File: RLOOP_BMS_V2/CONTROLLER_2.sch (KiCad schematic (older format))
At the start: 20 parts, among them IC3 ATA6870N-PLQW-1

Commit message: Footprint work
starting to assign footprints to parts
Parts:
- C10, C11, C12, C13, C14, C15, C3, C4, C5, C6, C7, C8, C9: footprint (none) -> Capacitors_SMD:C_0603
- R10, R11, R8, R9: footprint (none) -> Resistors_SMD:R_0603
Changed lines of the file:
@@
 F 0 "C8" H 8100 1950 50  0000 L CNN
 F 1 "100 nF / 50V/ 10% / SMD 0603" H 8500 1950 50  0000 L CNN
-F 2 "" H 8388 1800 50  0001 C CNN
+F 2 "Capacitors_SMD:C_0603" H 8388 1800 50  0001 C CNN
 F 3 "" H 8350 1950 50  0001 C CNN
 	1    8350 1950
@@
 F 0 "C9" H 8100 2250 50  0000 L CNN
 F 1 "100 nF / 50V/ 10% / SMD 0603" H 8500 2250 50  0000 L CNN
-F 2 "" H 8388 2100 50  0001 C CNN
+F 2 "Capacitors_SMD:C_0603" H 8388 2100 50  0001 C CNN
 F 3 "" H 8350 2250 50  0001 C CNN
 	1    8350 2250
@@
 F 0 "C10" H 8100 2550 50  0000 L CNN
 F 1 "100 nF / 50V/ 10% / SMD 0603" H 8500 2550 50  0000 L CNN
-F 2 "" H 8388 2400 50  0001 C CNN
+F 2 "Capacitors_SMD:C_0603" H 8388 2400 50  0001 C CNN
 F 3 "" H 8350 2550 50  0001 C CNN
 	1    8350 2550
@@
 F 0 "C11" H 8100 2850 50  0000 L CNN
 F 1 "100 nF / 50V/ 10% / SMD 0603" H 8500 2850 50  0000 L CNN
-F 2 "" H 8388 2700 50  0001 C CNN
+F 2 "Capacitors_SMD:C_0603" H 8388 2700 50  0001 C CNN
 F 3 "" H 8350 2850 50  0001 C CNN
 	1    8350 2850
@@
 F 0 "C12" H 8100 3150 50  0000 L CNN
 F 1 "100 nF / 50V/ 10% / SMD 0603" H 8500 3150 50  0000 L CNN
-F 2 "" H 8388 3000 50  0001 C CNN
+F 2 "Capacitors_SMD:C_0603" H 8388 3000 50  0001 C CNN
 F 3 "" H 8350 3150 50  0001 C CNN
 	1    8350 3150
@@
 F 0 "C13" H 8100 3450 50  0000 L CNN
 F 1 "100 nF / 50V/ 10% / SMD 0603" H 8500 3450 50  0000 L CNN
-F 2 "" H 8388 3300 50  0001 C CNN
+F 2 "Capacitors_SMD:C_0603" H 8388 3300 50  0001 C CNN
 F 3 "" H 8350 3450 50  0001 C CNN
 	1    8350 3450
@@
 F 0 "R9" V 6980 4350 50  0000 C CNN
 F 1 "121K / 0.1W / 1% / SMD 0603" V 7050 4850 50  0000 C CNN
-F 2 "" V 6830 4350 50  0001 C CNN
+F 2 "Resistors_SMD:R_0603" V 6830 4350 50  0001 C CNN
 F 3 "" H 6900 4350 50  0001 C CNN
 	1    6900 4350
@@
 F 0 "R11" V 10030 4050 50  0000 C CNN
 F 1 "10K / .1 W / 1% / SMD 0603" H 9300 4050 50  0000 C CNN
-F 2 "" V 9880 4050 50  0001 C CNN
+F 2 "Resistors_SMD:R_0603" V 9880 4050 50  0001 C CNN
 F 3 "" H 9950 4050 50  0001 C CNN
 	1    9950 4050
@@
 F 0 "R10" V 9080 4050 50  0000 C CNN
 F 1 "10K / .1 W / 1% / SMD 0603" H 9200 4200 50  0000 C CNN
-F 2 "" V 8930 4050 50  0001 C CNN
+F 2 "Resistors_SMD:R_0603" V 8930 4050 50  0001 C CNN
 F 3 "" H 9000 4050 50  0001 C CNN
 	1    9000 4050
@@
 F 0 "C15" H 9575 4650 50  0000 L CNN
 F 1 "100n" H 9250 4550 50  0000 L CNN
-F 2 "" H 9588 4400 50  0001 C CNN
+F 2 "Capacitors_SMD:C_0603" H 9588 4400 50  0001 C CNN
 F 3 "" H 9550 4550 50  0001 C CNN
 	1    9550 4550
@@
 F 0 "C14" H 8475 4650 50  0000 L CNN
 F 1 "100n" H 8200 4450 50  0000 L CNN
-F 2 "" H 8488 4400 50  0001 C CNN
+F 2 "Capacitors_SMD:C_0603" H 8488 4400 50  0001 C CNN
 F 3 "" H 8450 4550 50  0001 C CNN
 	1    8450 4550
@@
 F 0 "R8" V 2730 6900 50  0000 C CNN
 F 1 "10" V 2650 6900 50  0000 C CNN
-F 2 "" V 2580 6900 50  0001 C CNN
+F 2 "Resistors_SMD:R_0603" V 2580 6900 50  0001 C CNN
 F 3 "" H 2650 6900 50  0001 C CNN
 	1    2650 6900
@@
 F 0 "C7" H 6775 2100 50  0000 L CNN
 F 1 "100nF / 50V / 10% / SMD 0603" H 5400 2150 50  0000 L CNN
-F 2 "" H 6788 1850 50  0001 C CNN
+F 2 "Capacitors_SMD:C_0603" H 6788 1850 50  0001 C CNN
 F 3 "" H 6750 2000 50  0001 C CNN
 	1    6750 2000
@@
 F 0 "C4" H 3225 7250 50  0000 L CNN
 F 1 "10uF / 25V / 20% / SMD 1206" H 1750 7150 50  0000 L CNN
-F 2 "" H 3238 7000 50  0001 C CNN
+F 2 "Capacitors_SMD:C_0603" H 3238 7000 50  0001 C CNN
 F 3 "" H 3200 7150 50  0001 C CNN
 	1    3200 7150
@@
 F 0 "C6" H 5475 1800 50  0000 L CNN
 F 1 "100n / 50V / 10% / SMD 0603" H 5250 1900 50  0000 L CNN
-F 2 "" H 5488 1550 50  0001 C CNN
+F 2 "Capacitors_SMD:C_0603" H 5488 1550 50  0001 C CNN
 F 3 "" H 5450 1700 50  0001 C CNN
 	1    5450 1700
@@
 F 0 "C5" H 3275 2900 50  0000 L CNN
 F 1 "100nF / 50V / 10% / SMD 0603" H 3275 2700 50  0000 L CNN
-F 2 "" H 3288 2650 50  0001 C CNN
+F 2 "Capacitors_SMD:C_0603" H 3288 2650 50  0001 C CNN
 F 3 "" H 3250 2800 50  0001 C CNN
 	1    3250 2800
@@
 F 0 "C3" H 2725 2900 50  0000 L CNN
 F 1 "10uF / 25V / 20% / SMD 1206" H 1300 2800 50  0000 L CNN
-F 2 "" H 2738 2650 50  0001 C CNN
+F 2 "Capacitors_SMD:C_0603" H 2738 2650 50  0001 C CNN
 F 3 "" H 2700 2800 50  0001 C CNN
 	1    2700 2800

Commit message: footprint and layout work WIP
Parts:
- IC3: footprint (none) -> rLoop_Footprints:ATA6870-QFN48
- TH1, TH2: footprint (none) -> Resistors_SMD:R_0603
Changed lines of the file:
@@
 F 0 "IC3" H 6300 5200 60  0000 C CNN
 F 1 "ATA6870N-PLQW-1" H 6650 5100 60  0000 C CNN
-F 2 "" H 5550 3400 60  0001 C CNN
+F 2 "rLoop_Footprints:ATA6870-QFN48" H 5550 3400 60  0001 C CNN
 F 3 "" H 5550 3400 60  0001 C CNN
 	1    5600 3400
@@
 F 0 "TH2" V 9775 4550 50  0000 C CNN
 F 1 "NTCS0603E3103JLT" H 10450 4550 50  0000 C CNN
-F 2 "" H 9950 4600 50  0001 C CNN
+F 2 "Resistors_SMD:R_0603" H 9950 4600 50  0001 C CNN
 F 3 "" H 9950 4600 50  0001 C CNN
 	1    9950 4550
@@
 F 0 "TH1" V 8825 4550 50  0000 C CNN
 F 1 "NTCS0603E3103JLT" H 9000 4350 50  0000 C CNN
-F 2 "" H 9000 4600 50  0001 C CNN
+F 2 "Resistors_SMD:R_0603" H 9000 4600 50  0001 C CNN
 F 3 "" H 9000 4600 50  0001 C CNN
 	1    9000 4550

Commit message: board layout wip
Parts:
- C3, C4: footprint Capacitors_SMD:C_0603 -> Capacitors_SMD:C_1206
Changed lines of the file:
@@
 F 0 "C4" H 3225 7250 50  0000 L CNN
 F 1 "10uF / 25V / 20% / SMD 1206" H 1750 7150 50  0000 L CNN
-F 2 "Capacitors_SMD:C_0603" H 3238 7000 50  0001 C CNN
+F 2 "Capacitors_SMD:C_1206" H 3238 7000 50  0001 C CNN
 F 3 "" H 3200 7150 50  0001 C CNN
 	1    3200 7150
@@
 F 0 "C3" H 2725 2900 50  0000 L CNN
 F 1 "10uF / 25V / 20% / SMD 1206" H 1300 2800 50  0000 L CNN
-F 2 "Capacitors_SMD:C_0603" H 2738 2650 50  0001 C CNN
+F 2 "Capacitors_SMD:C_1206" H 2738 2650 50  0001 C CNN
 F 3 "" H 2700 2800 50  0001 C CNN
 	1    2700 2800

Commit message: WIP
See if it's even possible
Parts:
- removed C14, C15: 100n, Capacitors_SMD:C_0603, symbol C
- removed C5, C7: 100nF / 50V / 10% / SMD 0603, Capacitors_SMD:C_0603, symbol C
- removed C6: 100n / 50V / 10% / SMD 0603, Capacitors_SMD:C_0603, symbol C
- removed IC3: ATA6870N-PLQW-1, rLoop_Footprints:ATA6870-QFN48, symbol ATA6870N-PLQW-1
- removed R10, R11: 10K / .1 W / 1% / SMD 0603, Resistors_SMD:R_0603, symbol R
- removed R8: 10, Resistors_SMD:R_0603, symbol R
- removed R9: 121K / 0.1W / 1% / SMD 0603, Resistors_SMD:R_0603, symbol R
- removed TH1, TH2: NTCS0603E3103JLT, Resistors_SMD:R_0603, symbol Thermistor_NTC
- added U2: bq76PL536A_HTQFP, symbol bq76PL536A_HTQFP
- C3, C4: value 10uF / 25V / 20% / SMD 1206 -> 2.2 uF / 50V/ 10% / SMD 0603; footprint Capacitors_SMD:C_1206 -> (none)
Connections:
- net labels added: 5V_2, CS_N, CS_S, SCLK_N, SCLK_S, SDI_N, SDI_S, SDO_N, SDO_S
- net labels removed: CLK_IN, CLK_OUT, IRQ_IN, IRQ_OUT, SPI_MISO_LWR, SPI_MISO_UP, SPI_MOSI_LWR, SPI_MOSI_UP, SPI_NCS_LWR, SPI_NCS_UP, SPI_SCK_LWR, SPI_SCK_UP, VDDHVM, VDDHVP, ~PD_IN, ~PD_OUT
- wire segments 86 -> 52
- no-connect marks 3 -> 9
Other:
- moved on the sheet: C10, C11, C12, C13, C8, C9

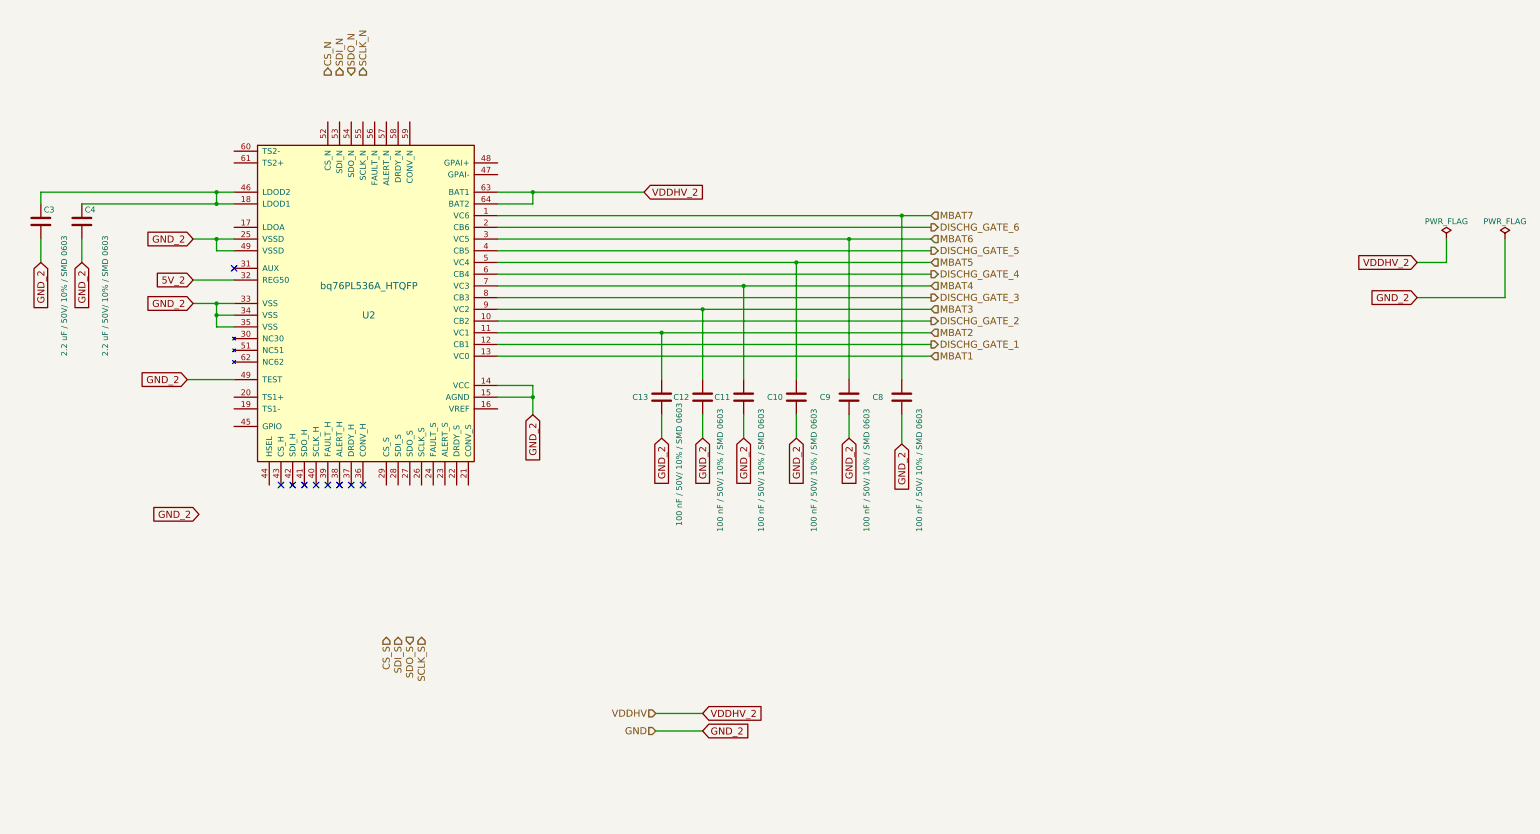
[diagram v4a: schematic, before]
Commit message: Ti BMS WIP
Getting there. Need to add temp sensors, fan control, and an LDO for the
SPI ISO supply.
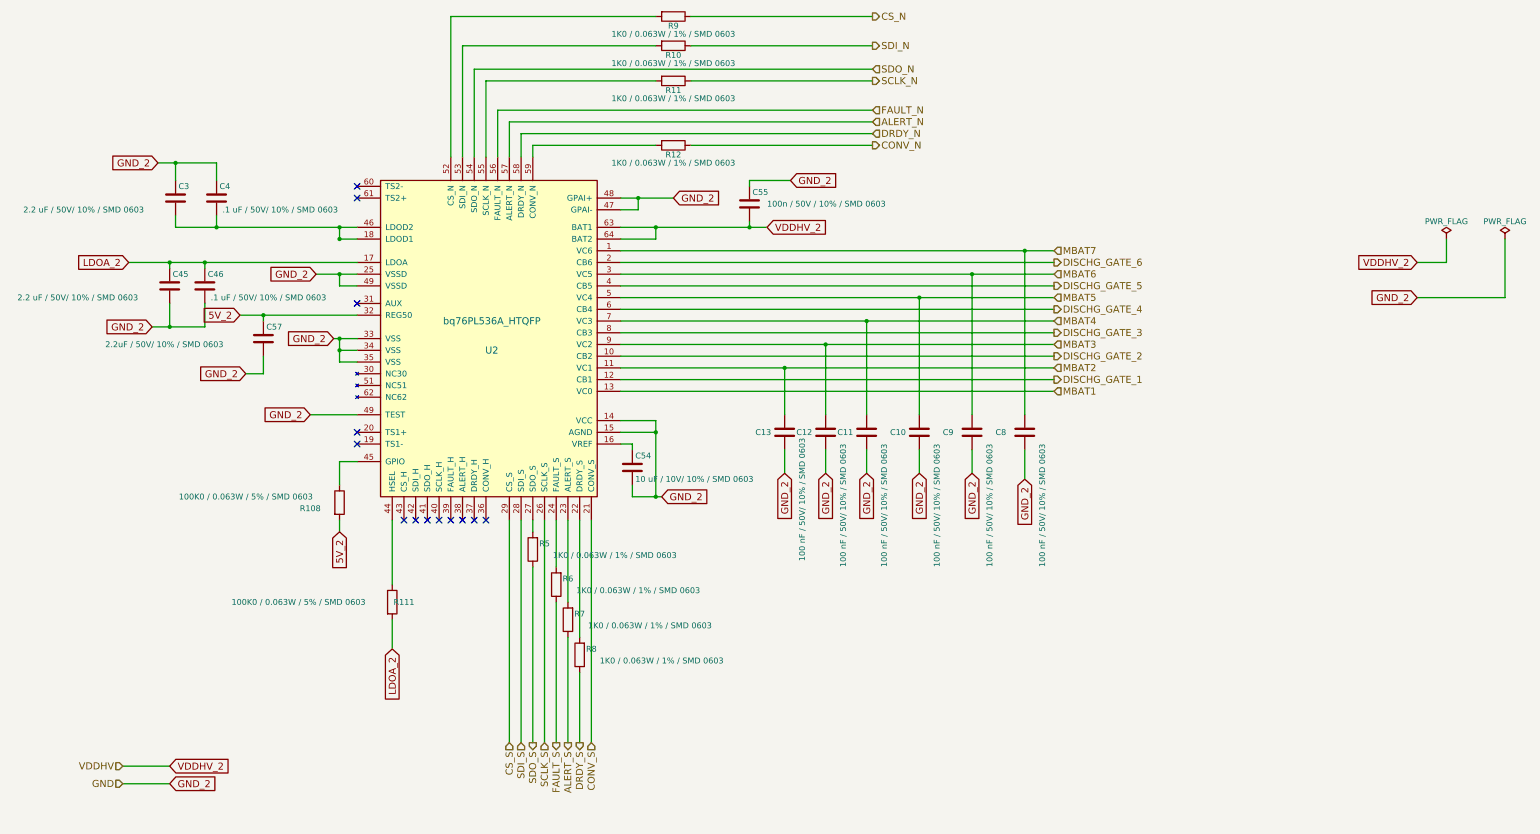
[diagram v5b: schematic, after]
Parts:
- added C45: 2.2 uF / 50V/ 10% / SMD 0603, Capacitors_SMD:C_0603, symbol C
- added C46: .1 uF / 50V/ 10% / SMD 0603, Capacitors_SMD:C_0603, symbol C
- added C54: 10 uF / 10V/ 10% / SMD 0603, Capacitors_SMD:C_0603, symbol C
- added C55: 100n / 50V / 10% / SMD 0603, Capacitors_SMD:C_0603, symbol C
- added C57: 2.2uF / 50V/ 10% / SMD 0603, Capacitors_SMD:C_0603, symbol C
- added R10, R11, R12, R5, R6, R7, R8, R9: 1K0 / 0.063W / 1% / SMD 0603, Resistors_SMD:R_0603, symbol R
- added R108, R111: 100K0 / 0.063W / 5% / SMD 0603, Resistors_SMD:R_0603, symbol R
- C3: footprint (none) -> Capacitors_SMD:C_0603
- C4: value 2.2 uF / 50V/ 10% / SMD 0603 -> .1 uF / 50V/ 10% / SMD 0603; footprint (none) -> Capacitors_SMD:C_0603
- U2: footprint (none) -> rLoop_Footprints:bq76pl536a
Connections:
- net 5V_2: now also C57.1, R108.2
- net CS_N: now also R9.1
- net CS_S: now also U2.29 (CS_S)
- net GND_2: now also C3.1, C4.1, U2.47 (GPAI-), U2.48 (GPAI+), C45.2, C46.2, C54.2, C55.1, C57.2; no longer C3.2, C4.2
- net SCLK_N: now also R11.1
- net SCLK_S: now also U2.26 (SCLK_S)
- net SDI_N: now also R10.1
- net SDI_S: now also U2.28 (SDI_S)
- net SDO_N: now also U2.54 (SDO_N)
- net SDO_S: now also R5.1
- net VDDHV_2: now also C55.2
- net at U2.16 (VREF): now also C54.1
- net LDOA_2: now reaches U2.17 (LDOA)
- net LDOA_2: now also C45.1, C46.1, R111.2
- net at U2.18 (LDOD1), U2.46 (LDOD2): now also C3.2, C4.2; no longer C3.1, C4.1
- net CONV_S: now reaches U2.21 (CONV_S)
- net at U2.22 (DRDY_S): now also R8.2
- net at U2.23 (ALERT_S): now also R7.2
- net at U2.24 (FAULT_S): now also R6.2
- net at U2.27 (SDO_S): now also R5.2
- net at U2.44 (HSEL): now also R111.1
- net at U2.45 (GPIO): now also R108.1
- net at U2.52 (CS_N): now also R9.2
- net at U2.53 (SDI_N): now also R10.2
- net at U2.55 (SCLK_N): now also R11.2
- net FAULT_N: now reaches U2.56 (FAULT_N)
- net ALERT_N: now reaches U2.57 (ALERT_N)
- net DRDY_N: now reaches U2.58 (DRDY_N)
- net at U2.59 (CONV_N): now also R12.2
- new net ALERT_S: R7.1
- new net CONV_N: R12.1
- new net DRDY_S: R8.1
- new net FAULT_S: R6.1
- no-connect marks 9 -> 13
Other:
- moved on the sheet: C10, C11, C12, C13, C3, C4, C8, C9, U2

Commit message: More WIP on BMS v2.5
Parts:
- added C? (x2): .047 uF / 50V/ 10% / SMD 0603, Capacitors_SMD:C_0603, symbol C
- added R? (x4): 1.82k / 0.063W / 1% / SMD0603, symbol R
- added TH? (x2): 10k / 1% / 3454K / SMD0603, symbol Thermistor_NTC
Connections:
- net 5V_2: now also C?.1, C?.2, TH?.1, TH?.2
- net at U2.19 (TS1-): now also R?.1
- net at U2.20 (TS1+): now also C?.1, R?.1, R?.2
- net at U2.60 (TS2-): now also R?.1
- net at U2.61 (TS2+): now also C?.2, R?.1, R?.2
- new net: R?.2, TH?.2
- new net: R?.2, TH?.1
- no-connect marks 13 -> 9
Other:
- moved on the sheet: C10, C11, C12, C13, C3, C4, C45, C46, C54, C55, C57, C8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

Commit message: More BMS v2.5 WIP
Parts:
- R116, R117, R118, R119: renamed from R?; footprint (none) -> Resistors_SMD:R_0603
- TH3, TH4: renamed from TH?; footprint (none) -> Resistors_SMD:R_0603
- gave numbers to parts that had none: 2
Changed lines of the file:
@@
 $Descr A4 11693 8268
 encoding utf-8
-Sheet 5 9
+Sheet 5 10
 Title ""
 Date ""
@@
 $EndComp
 $Comp
-L C C?
+L C C61
 U 1 1 592E67EF
 P 3550 1650
-F 0 "C?" H 3575 1750 50  0000 L CNN
+F 0 "C61" H 3575 1750 50  0000 L CNN
 F 1 ".047 uF / 50V/ 10% / SMD 0603" H 3600 1550 50  0000 L CNN
 F 2 "Capacitors_SMD:C_0603" H 3588 1500 50  0001 C CNN
@@
 $EndComp
 $Comp
-L R R?
+L R R119
 U 1 1 592E68AE
 P 4000 2200
-F 0 "R?" V 3900 2200 50  0000 C CNN
+F 0 "R119" V 3900 2200 50  0000 C CNN
 F 1 "1.82k / 0.063W / 1% / SMD0603" V 3800 2500 50  0000 C CNN
-F 2 "" V 3930 2200 50  0001 C CNN
+F 2 "Resistors_SMD:R_0603" V 3930 2200 50  0001 C CNN
 F 3 "" H 4000 2200 50  0001 C CNN
 	1    4000 2200
@@
 $EndComp
 $Comp
-L R R?
+L R R118
 U 1 1 592E6D61
 P 3350 2200
-F 0 "R?" V 3450 2200 50  0000 C CNN
+F 0 "R118" V 3450 2200 50  0000 C CNN
 F 1 "1.82k / 0.063W / 1% / SMD0603" V 3550 2550 50  0000 C CNN
-F 2 "" V 3280 2200 50  0001 C CNN
+F 2 "Resistors_SMD:R_0603" V 3280 2200 50  0001 C CNN
 F 3 "" H 3350 2200 50  0001 C CNN
 	1    3350 2200
@@
 $EndComp
 $Comp
-L Thermistor_NTC TH?
+L Thermistor_NTC TH4
 U 1 1 592E75DB
 P 3150 1650
-F 0 "TH?" H 2900 1700 50  0000 C CNN
+F 0 "TH4" H 2900 1700 50  0000 C CNN
 F 1 "10k / 1% / 3454K / SMD0603" H 2350 1600 50  0000 C CNN
-F 2 "" H 3150 1700 50  0001 C CNN
+F 2 "Resistors_SMD:R_0603" H 3150 1700 50  0001 C CNN
 F 3 "" H 3150 1700 50  0001 C CNN
 	1    3150 1650
@@
 Connection ~ 3150 1300
 $Comp
-L R R?
+L R R117
 U 1 1 592E7F7D
 P 2550 4400
-F 0 "R?" V 2650 4400 50  0000 C CNN
+F 0 "R117" V 2650 4400 50  0000 C CNN
 F 1 "1.82k / 0.063W / 1% / SMD0603" V 2750 5000 50  0000 C CNN
-F 2 "" V 2480 4400 50  0001 C CNN
+F 2 "Resistors_SMD:R_0603" V 2480 4400 50  0001 C CNN
 F 3 "" H 2550 4400 50  0001 C CNN
 	1    2550 4400
@@
 $EndComp
 $Comp
-L R R?
+L R R116
 U 1 1 592E80EA
 P 2050 4400
-F 0 "R?" V 1950 4400 50  0000 C CNN
+F 0 "R116" V 1950 4400 50  0000 C CNN
 F 1 "1.82k / 0.063W / 1% / SMD0603" V 1850 3900 50  0000 C CNN
-F 2 "" V 1980 4400 50  0001 C CNN
+F 2 "Resistors_SMD:R_0603" V 1980 4400 50  0001 C CNN
 F 3 "" H 2050 4400 50  0001 C CNN
 	1    2050 4400
@@
 $EndComp
 $Comp
-L Thermistor_NTC TH?
+L Thermistor_NTC TH3
 U 1 1 592E82B0
 P 1900 4850
-F 0 "TH?" H 1650 4900 50  0000 C CNN
+F 0 "TH3" H 1650 4900 50  0000 C CNN
 F 1 "10k / 1% / 3454K / SMD0603" H 1100 4800 50  0000 C CNN
-F 2 "" H 1900 4900 50  0001 C CNN
+F 2 "Resistors_SMD:R_0603" H 1900 4900 50  0001 C CNN
 F 3 "" H 1900 4900 50  0001 C CNN
 	1    1900 4850
@@
 	2700 4400 4250 4400
 $Comp
-L C C?
+L C C60
 U 1 1 592E88B7
 P 2300 4850
-F 0 "C?" H 2325 4950 50  0000 L CNN
+F 0 "C60" H 2325 4950 50  0000 L CNN
 F 1 ".047 uF / 50V/ 10% / SMD 0603" H 2350 4750 50  0000 L CNN
 F 2 "Capacitors_SMD:C_0603" H 2338 4700 50  0001 C CNN
